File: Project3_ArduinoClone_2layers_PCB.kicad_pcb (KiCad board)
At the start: 2 copper layers, 40.1 x 26.4 mm, 17 parts, among them J1 Serial, J2 Digital pins, J3 ICSP, J4 I2C, U1 24LC1025, U2 24LC1025, U3 DS1337_v1, U4 ATMEGA328P-AU, Y1 Crystal 32 MHz, Y2 Crystal 16 MHz

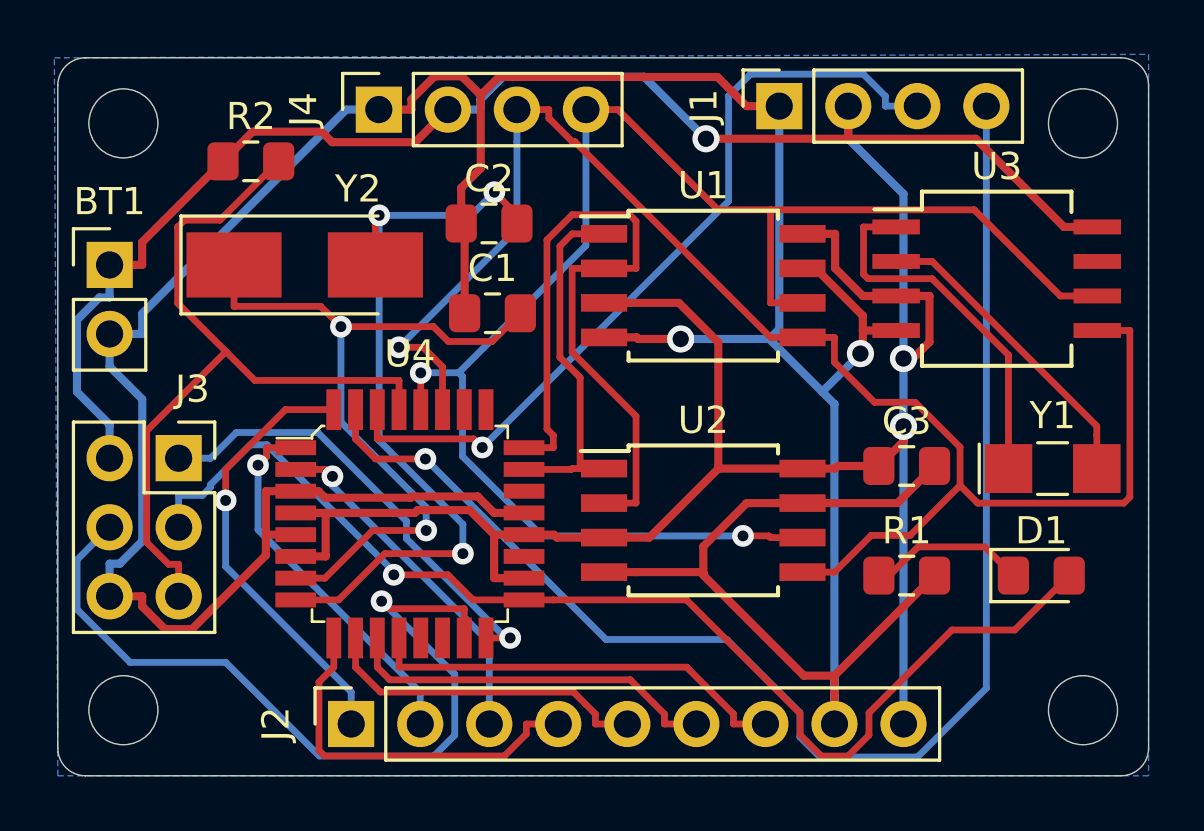
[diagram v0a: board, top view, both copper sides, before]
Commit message: Autoroute 2 and 4 layer version
Save different pcbnew files for each version
Create copper zone in 2 layer version,
and that is the main pcbnew file.
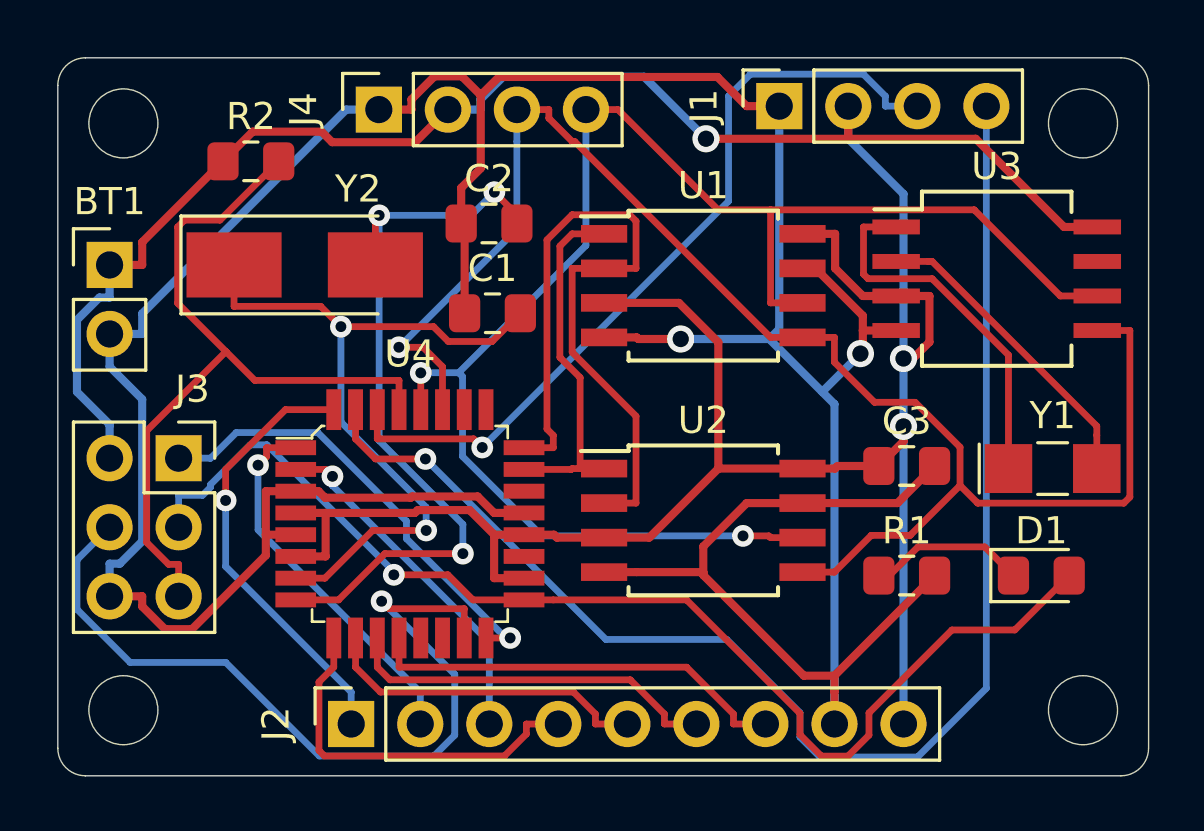
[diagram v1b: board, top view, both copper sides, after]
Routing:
- removed copper zone on B.Cu, net GND
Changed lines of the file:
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@@
   (layers
     (0 F.Cu signal)
-    (31 B.Cu signal)
+    (31 B.Cu mixed)
     (32 B.Adhes user)
     (33 F.Adhes user)
@@
   (segment (start 108.441 127.635) (end 109.6413 127.635) (width 0.25) (layer F.Cu) (net 24))
   (segment (start 115.824 135.255) (end 115.824 134.0297) (width 0.25) (layer F.Cu) (net 24))
-  (zone (net 2) (net_name GND) (layer B.Cu) (hatch edge 0.508)
-    (connect_pads (clearance 0.508))
-    (min_thickness 0.254)
-    (fill yes (arc_segments 32) (thermal_gap 0.508) (thermal_bridge_width 0.508))
-    (polygon
-      (pts
-        (xy 77.47 120.142) (xy 117.729 120.015) (xy 117.729 146.558) (xy 77.597 146.558)
-      )
-    )
-  )
 )
